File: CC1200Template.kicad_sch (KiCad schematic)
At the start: 39 parts, among them J1 Conn_Coaxial, J3002 RFShield_OnePiece, U1 CC1200, Y2 40 MHz

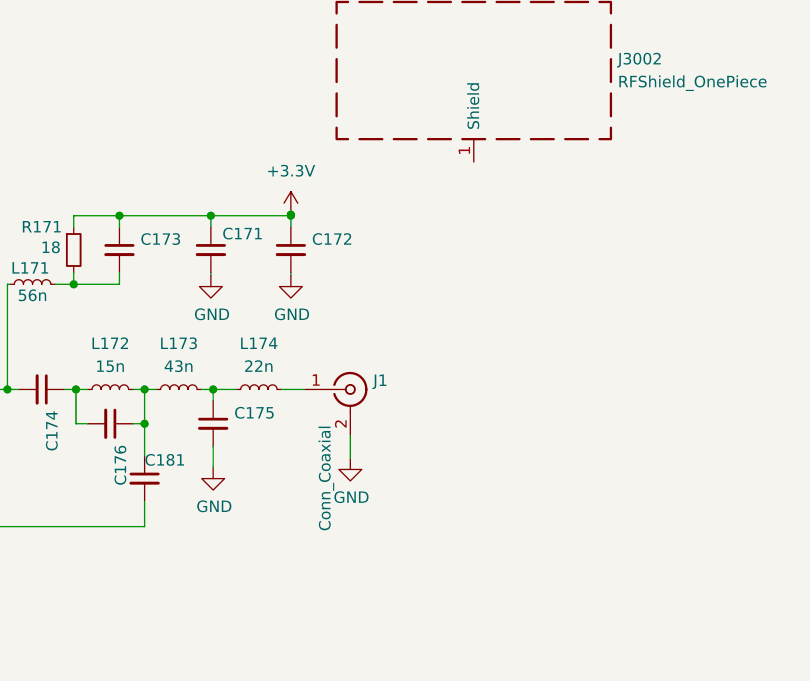
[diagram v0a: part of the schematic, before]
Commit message: fix clearance issues & errors in footprints and add vias for ground and add ground and vcc pours
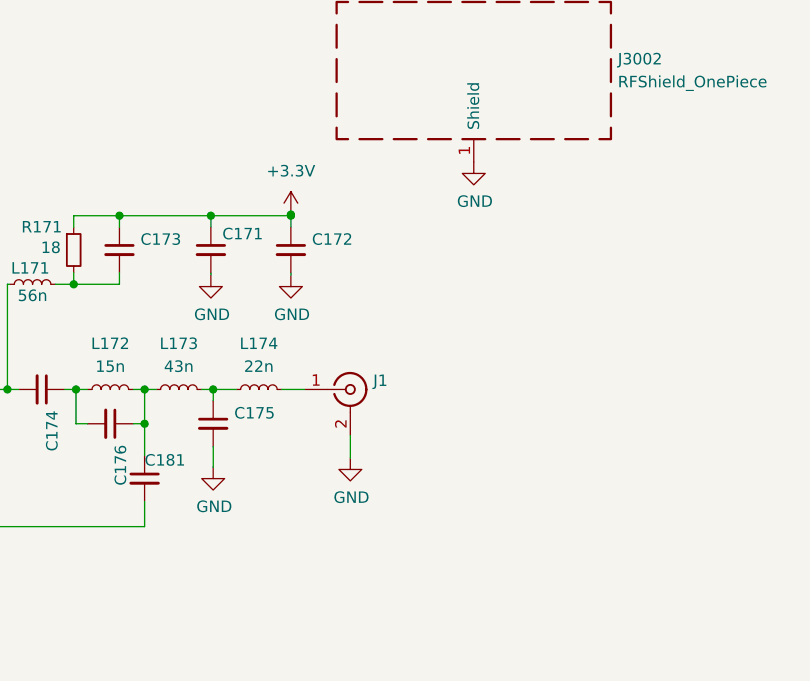
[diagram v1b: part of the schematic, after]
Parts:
- J1: value Conn_Coaxial -> (none); footprint Connector_Coaxial:SMA_Amphenol_901-143_Horizontal -> (none)
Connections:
- net GND: now also J3002.1 (Shield)
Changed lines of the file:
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@@
       (effects (font (size 1.27 1.27)) (justify left))
     )
-    (property "Value" "Conn_Coaxial" (id 1) (at 207.772 90.805 90)
-      (effects (font (size 1.27 1.27)) (justify left))
-    )
-    (property "Footprint" "Connector_Coaxial:SMA_Amphenol_901-143_Horizontal" (id 2) (at 210.566 75.057 0)
+    (property "Value" "" (id 1) (at 207.772 90.805 90)
+      (effects (font (size 1.27 1.27)) (justify left))
+    )
+    (property "Footprint" "" (id 2) (at 210.566 75.057 0)
       (effects (font (size 1.27 1.27)) hide)
     )
@@
     (pin "1")
     (pin "2")
+  )
+  (symbol (lib_id "power:GND") (at 224.282 49.784 0) (unit 1)
+    (in_bom yes) (on_board yes)
+    (property "Reference" "#PWR?" (id 0) (at 224.282 56.134 0)
+      (effects (font (size 1.27 1.27)) hide)
+    )
+    (property "Value" "GND" (id 1) (at 224.409 54.1782 0))
+    (property "Footprint" "" (id 2) (at 224.282 49.784 0)
+      (effects (font (size 1.27 1.27)) hide)
+    )
+    (property "Datasheet" "" (id 3) (at 224.282 49.784 0)
+      (effects (font (size 1.27 1.27)) hide)
+    )
+    (pin "1")
   )
   (symbol (lib_id "power:GND") (at 133.858 70.739 0) (unit 1)
@@
       (reference "#PWR0124") (unit 1) (value "GND") (footprint "")
     )
+    (path "/bf6d775b-672a-46e5-bd45-fb6d8187cfea"
+      (reference "#PWR?") (unit 1) (value "GND") (footprint "")
+    )
     (path "/e9401fd4-c572-4b85-a808-d25b6191ddb8"
-      (reference "C10") (unit 1) (value "12p") (footprint "Capacitor_SMD:C_0201_0603Metric")
+      (reference "C10") (unit 1) (value "12p") (footprint "Capacitor_SMD:C_0603_1608Metric")
     )
     (path "/63cecbcb-a4a2-43fe-8a97-acdbd1903604"
-      (reference "C11") (unit 1) (value "12p") (footprint "Capacitor_SMD:C_0201_0603Metric")
+      (reference "C11") (unit 1) (value "12p") (footprint "Capacitor_SMD:C_0603_1608Metric")
     )
     (path "/bf4d2769-3e7f-4d1b-983b-b4c7bc8ab936"
@@
     )
     (path "/48aa441c-2fc6-43bf-b712-a7de6e65103d"
-      (reference "C25") (unit 1) (value "47n") (footprint "Capacitor_SMD:C_0201_0603Metric")
+      (reference "C25") (unit 1) (value "47n") (footprint "Capacitor_SMD:C_0603_1608Metric")
     )
     (path "/d51b6175-6cc6-4a96-9603-52c532709165"
@@
     )
     (path "/7fc6832d-554d-4ce3-b19f-8c72aa94229e"
-      (reference "C27") (unit 1) (value "10n") (footprint "Capacitor_SMD:C_01005_0402Metric")
+      (reference "C27") (unit 1) (value "10n") (footprint "Capacitor_SMD:C_0402_1005Metric")
     )
     (path "/3eda0a96-5e72-47fe-adcc-05505b64794f"
@@
     )
     (path "/04cb3c7b-c7b5-45cc-ae7b-2ef469daf5ab"
-      (reference "J1") (unit 1) (value "Conn_Coaxial") (footprint "Connector_Coaxial:SMA_Amphenol_901-143_Horizontal")
+      (reference "J1") (unit 1) (value "Conn_Coaxial") (footprint "Connector_Coaxial:HJ_Tech_SMA_Horizontal_Board_Edge_RF")
     )
     (path "/6925ae6e-508f-4623-a141-b4202f2a27bf"
